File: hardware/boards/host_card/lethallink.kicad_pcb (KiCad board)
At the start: 6 copper layers, 121.2 x 98.4 mm, 220 parts, among them J1 PCIe-x4, J2 USB3_Micro_B_Amphenol, J3 Conn_02x05_Odd_Even, J4 Conn_02x04_Odd_Even, J5 Conn_02x04_Odd_Even, J6 SODIMM_260, J7 Conn_02x04_Odd_Even, Q1 Q_NMOS_GSD, Q2 Q_NMOS_GSD, Q3 Q_NMOS_GSD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

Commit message: Fixed the missing bus connections to the FPGA for the USB3 PHY, and updated the PCB
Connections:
- U1 pad A2: /USB3 Interface/DQ12 -> /USB3 Interface/WE_D
- U1 pad A3: Net-(U1-PadA3) -> /USB3 Interface/DQ6
- U1 pad A4: Net-(U1-PadA4) -> /USB3 Interface/DQ0
- U1 pad A5: Net-(U1-PadA5) -> /USB3 Interface/DQ1
- U1 pad B1: /USB3 Interface/DQ13 -> /USB3 Interface/OE
- U1 pad B2: /USB3 Interface/DQ14 -> /USB3 Interface/ALE
- U1 pad B3: Net-(U1-PadB3) -> /USB3 Interface/DQ7
- U1 pad B4: Net-(U1-PadB4) -> /USB3 Interface/DQ5
- U1 pad B5: Net-(U1-PadB5) -> /USB3 Interface/DQ2
- U1 pad C1: /USB3 Interface/DQ8 -> Net-(U1-PadC1)
- U1 pad C2: /USB3 Interface/DQ15 -> Net-(U1-PadC2)
- U1 pad C3: Net-(U1-PadC3) -> /USB3 Interface/DQ10
- U1 pad C4: Net-(U1-PadC4) -> /USB3 Interface/DQ4
- U1 pad C5: Net-(U1-PadC5) -> /USB3 Interface/DQ3
- U1 pad D1: /USB3 Interface/DQ9 -> Net-(U1-PadD1)
- U1 pad D2: /USB3 Interface/DQ10 -> Net-(U1-PadD2)
- U1 pad D3: Net-(U1-PadD3) -> /USB3 Interface/DQ11
- U1 pad D5: Net-(U1-PadD5) -> /USB3 Interface/DQ9
- U1 pad E1: /USB3 Interface/DQ11 -> Net-(U1-PadE1)
- U1 pad E2: /USB3 Interface/DQ3 -> Net-(U1-PadE2)
- U1 pad E3: /USB3 Interface/OE -> /USB3 Interface/DQ13
- U1 pad E4: Net-(U1-PadE4) -> /USB3 Interface/DQ8
- U1 pad E5: /USB3 Interface/ALE -> /USB3 Interface/DQ14
- U1 pad F1: Net-(U1-PadF1) -> /AUX Control/WAKE#
- U1 pad F2: /USB3 Interface/DQ2 -> Net-(U1-PadF2)
- U1 pad F3: /USB3 Interface/DQ1 -> Net-(U1-PadF3)
- U1 pad F4: /USB3 Interface/WE_D -> /USB3 Interface/DQ12
- U1 pad F5: Net-(U1-PadF5) -> /USB3 Interface/DQ15
- U1 pad G1: Net-(U1-PadG1) -> /AUX Control/PCIe_TRST#
- U1 pad G2: Net-(U1-PadG2) -> /AUX Control/CLKREQ#
- U1 pad G3: /USB3 Interface/DQ0 -> Net-(U1-PadG3)
- U1 pad G5: /USB3 Interface/DQ5 -> Net-(U1-PadG5)
- U1 pad H2: Net-(U1-PadH2) -> /AUX Control/PERST#
- U1 pad H3: /USB3 Interface/DQ7 -> Net-(U1-PadH3)
- U1 pad H4: /USB3 Interface/DQ4 -> Net-(U1-PadH4)
- U1 pad H5: /USB3 Interface/DQ6 -> Net-(U1-PadH5)
- U1 pad J3: Net-(U1-PadJ3) -> /AUX Control/PCIe_SMCLK
- U1 pad J4: /AUX Control/PCIe_TMS -> Net-(U1-PadJ4)
- U1 pad J5: Net-(U1-PadJ5) -> /AUX Control/PCIe_SMDAT
- U1 pad K16: Net-(U1-PadK16) -> /DDR3 Cache/A6
- U1 pad K17: Net-(U1-PadK17) -> /DDR3 Cache/BA0
- U1 pad K4: /AUX Control/PCIe_TDO -> /AUX Control/PCIe_TCK
- U1 pad L1: /AUX Control/PCIe_SMCLK -> Net-(U1-PadL1)
- U1 pad L4: Net-(U1-PadL4) -> /AUX Control/PCIe_TDI
- U1 pad M1: /AUX Control/PCIe_SMDAT -> Net-(U1-PadM1)
- U1 pad M4: /AUX Control/PCIe_TCK -> /AUX Control/PCIe_TDO
- U1 pad N2: Net-(U1-PadN2) -> /AUX Control/PCIe_TMS
- U1 pad N4: /AUX Control/PCIe_TDI -> Net-(U1-PadN4)
- U1 pad P1: /AUX Control/CLKREQ# -> Net-(U1-PadP1)
- U1 pad P2: /AUX Control/WAKE# -> Net-(U1-PadP2)
- U1 pad P3: /AUX Control/PERST# -> Net-(U1-PadP3)
- U1 pad P4: /AUX Control/PCIe_TRST# -> Net-(U1-PadP4)

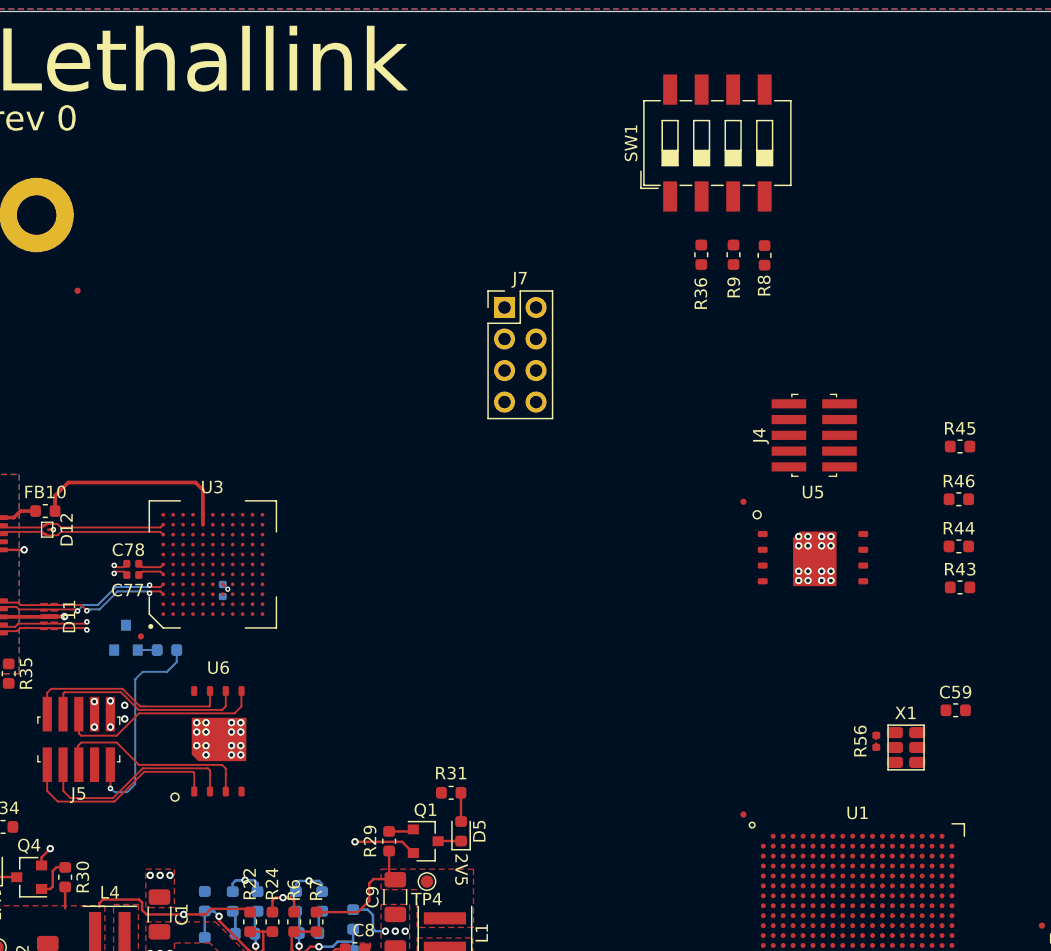
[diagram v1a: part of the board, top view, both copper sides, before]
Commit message: Swizzled the pins on the PHY bus to make routing to the FPGA nicer, also did the initial bus routing
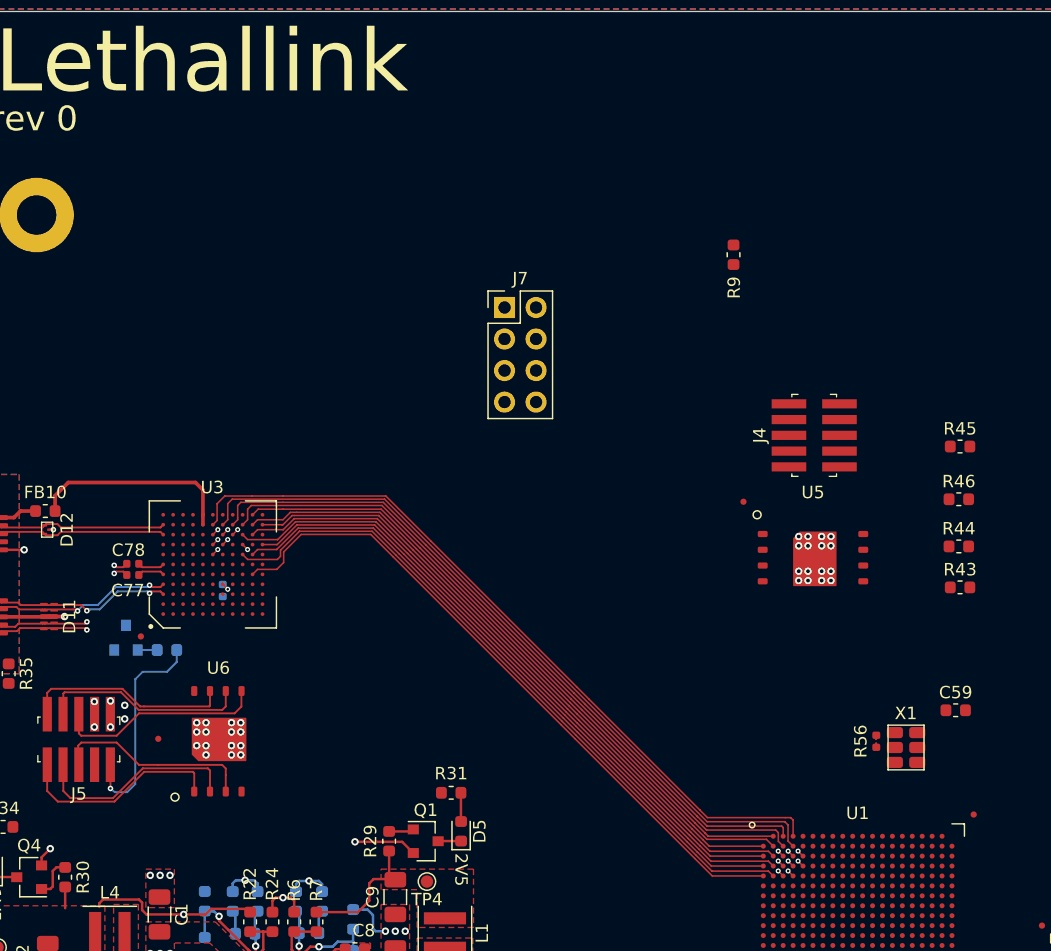
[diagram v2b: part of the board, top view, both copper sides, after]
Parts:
- removed R36, R8: 1k, Resistor_SMD:R_0603_1608Metric
- removed SW1: SW_DIP_x03, Button_Switch_SMD:SW_DIP_SPSTx04_Slide_6.7x11.72mm_W8.61mm_P2.54mm_LowProfile
- moved FID4 36.7 mm to (34.8, 74.3)
- moved FID3 18.5 mm to (100.5, 80.4)
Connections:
- U1 pad A2: /USB3 Interface/WE_D -> /USB3 Interface/DQ10
- U1 pad A5: /USB3 Interface/DQ1 -> Net-(U1-PadA5)
- U1 pad B1: /USB3 Interface/OE -> /USB3 Interface/DQ11
- U1 pad B2: /USB3 Interface/ALE -> /USB3 Interface/DQ12
- U1 pad B3: /USB3 Interface/DQ7 -> /USB3 Interface/DQ8
- U1 pad B4: /USB3 Interface/DQ5 -> /USB3 Interface/DQ3
- U1 pad B5: /USB3 Interface/DQ2 -> Net-(U1-PadB5)
- U1 pad C1: Net-(U1-PadC1) -> /USB3 Interface/DQ9
- U1 pad C2: Net-(U1-PadC2) -> /USB3 Interface/DQ13
- U1 pad C3: /USB3 Interface/DQ10 -> /USB3 Interface/DQ5
- U1 pad C4: /USB3 Interface/DQ4 -> /USB3 Interface/DQ7
- U1 pad C5: /USB3 Interface/DQ3 -> /USB3 Interface/DQ1
- U1 pad D1: Net-(U1-PadD1) -> /USB3 Interface/WE_D
- U1 pad D2: Net-(U1-PadD2) -> /Boot Config/~PHY_INT
- U1 pad D3: /USB3 Interface/DQ11 -> /USB3 Interface/DQ15
- U1 pad D5: /USB3 Interface/DQ9 -> /USB3 Interface/DQ4
- U1 pad E1: Net-(U1-PadE1) -> /USB3 Interface/ALE
- U1 pad E2: Net-(U1-PadE2) -> /USB3 Interface/OE
- U1 pad E3: /USB3 Interface/DQ13 -> /USB3 Interface/DQ14
- U1 pad E4: /USB3 Interface/DQ8 -> /USB3 Interface/DQ2
- U1 pad E5: /USB3 Interface/DQ14 -> Net-(U1-PadE5)
- U1 pad F4: /USB3 Interface/DQ12 -> Net-(U1-PadF4)
- U1 pad F5: /USB3 Interface/DQ15 -> Net-(U1-PadF5)
- U1 pad R4: Net-(R8-Pad2) -> GND
- U1 pad U4: Net-(R36-Pad2) -> GND
- U3 pad K8: /Boot Config/~PHY_INT -> Net-(U3-PadK8)
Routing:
- net /USB3 Interface/DQ0: track 0.00 -> 60.6 mm
- net /USB3 Interface/DQ1: track 0.00 -> 60.0 mm, vias 0 -> 2
- net /USB3 Interface/DQ3: track 0.00 -> 59.9 mm
- net /USB3 Interface/DQ4: track 0.00 -> 59.6 mm, vias 0 -> 2
- net /USB3 Interface/DQ2: track 0.00 -> 59.2 mm, vias 0 -> 2
- net /USB3 Interface/DQ5: track 0.00 -> 57.9 mm, vias 0 -> 2
- net /USB3 Interface/DQ6: track 0.00 -> 57.3 mm
- net /USB3 Interface/DQ15: track 0.00 -> 57.2 mm, vias 0 -> 2
- net /USB3 Interface/DQ7: track 0.00 -> 57.0 mm, vias 0 -> 2
- net /USB3 Interface/DQ8: track 0.00 -> 56.5 mm
- net /USB3 Interface/DQ14: track 0.00 -> 55.8 mm, vias 0 -> 2
- net /USB3 Interface/OE: track 0.00 -> 55.7 mm
- net /USB3 Interface/ALE: track 0.00 -> 54.4 mm
- net /USB3 Interface/DQ9: track 0.00 -> 53.9 mm
- net /USB3 Interface/DQ13: track 0.00 -> 53.7 mm
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
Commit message: Wiggling traces is hard
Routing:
- net /USB3 Interface/ALE: track 54.4 -> 39.6 mm
- net /USB3 Interface/DQ3: track 59.9 -> 47.6 mm
- net /USB3 Interface/DQ8: track 56.5 -> 45.9 mm
- net /USB3 Interface/OE: track 55.7 -> 46.8 mm
- net /USB3 Interface/DQ9: track 53.9 -> 45.4 mm
- net /Boot Config/~PHY_INT: track 53.2 -> 44.7 mm
- net /USB3 Interface/WE_D: track 53.3 -> 44.8 mm
- net /USB3 Interface/DQ6: track 57.3 -> 49.2 mm
- net /USB3 Interface/DQ12: track 53.5 -> 45.4 mm
- net /USB3 Interface/DQ11: track 51.7 -> 43.7 mm
- net /USB3 Interface/DQ13: track 53.7 -> 45.8 mm
- net /USB3 Interface/DQ10: track 53.1 -> 45.1 mm
- net /USB3 Interface/DQ0: track 60.6 -> 62.0 mm

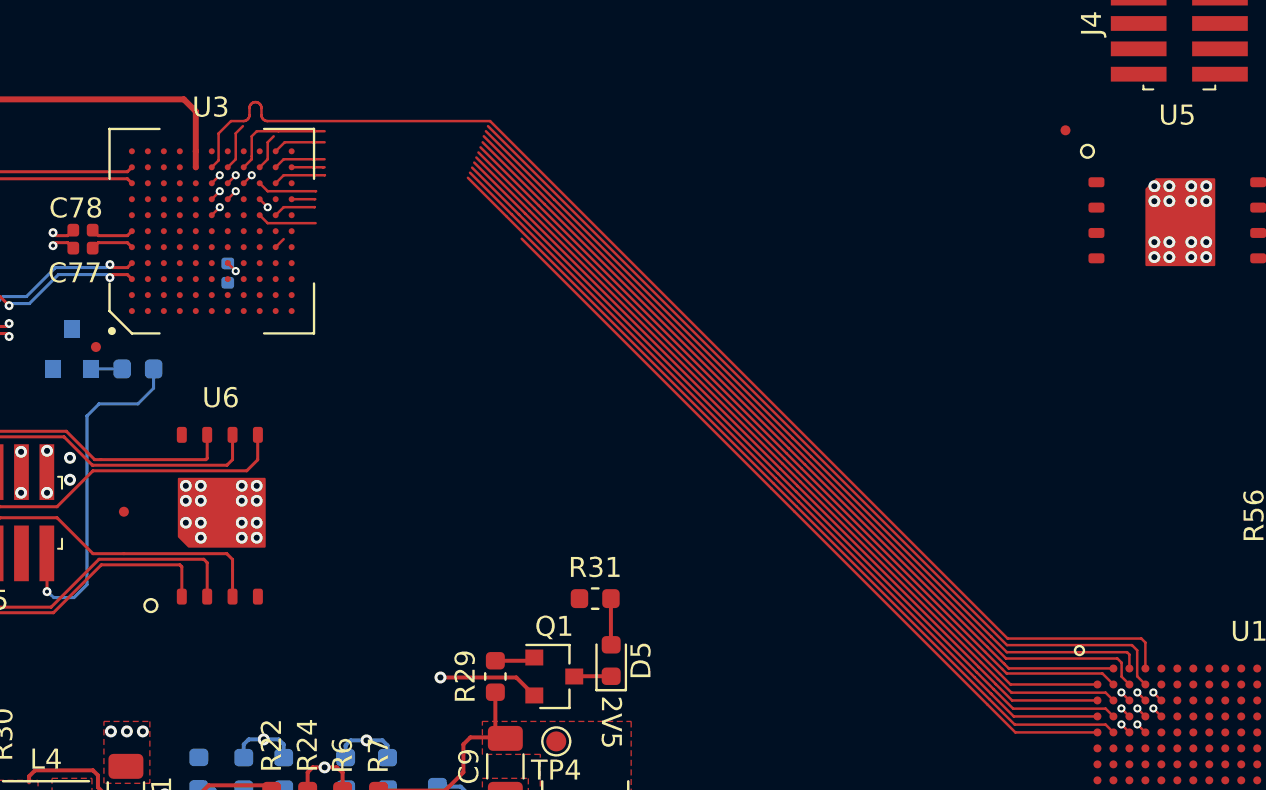
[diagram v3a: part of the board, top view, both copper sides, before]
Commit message: Created a suggested via layout for routing out the Cypress USB3 PHY
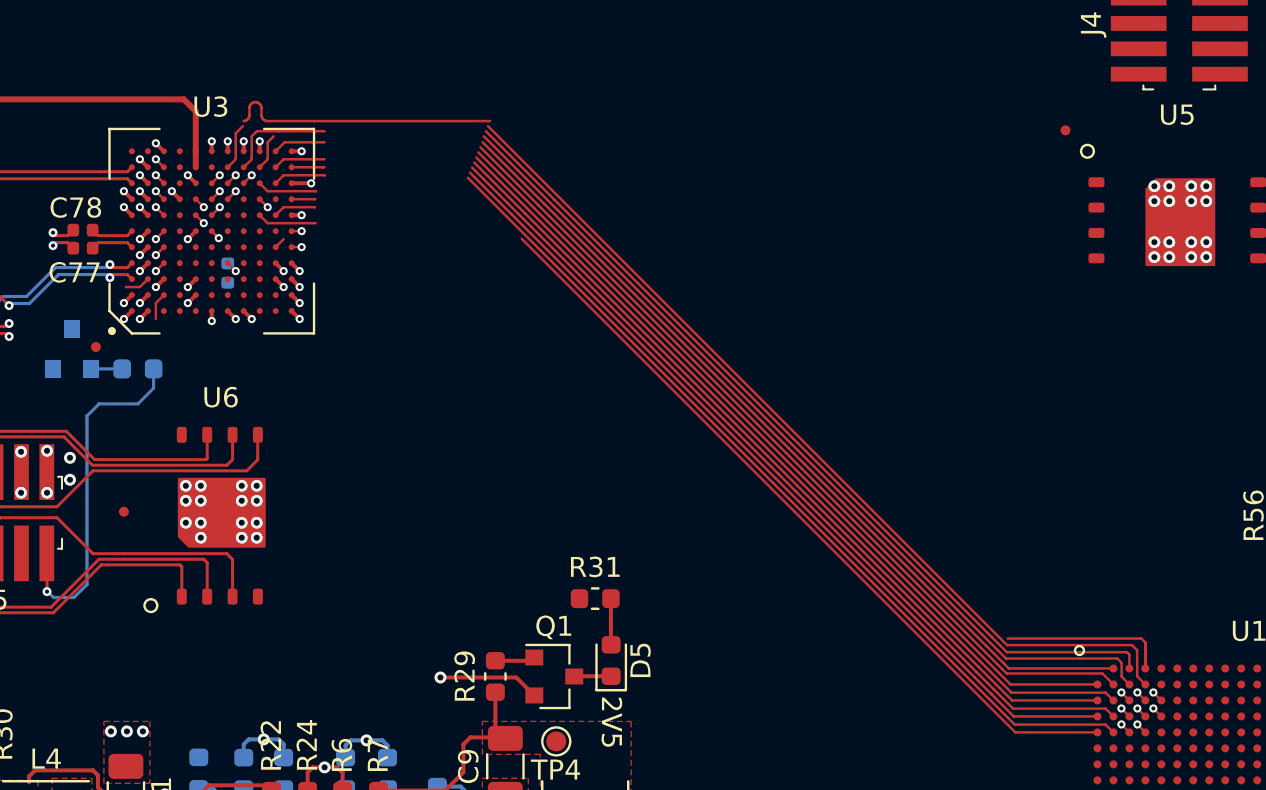
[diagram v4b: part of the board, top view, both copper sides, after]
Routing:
- net /USB3 Interface/DQ0: track 62.0 -> 23.3 mm
- net GND: track 64.6 -> 75.7 mm, vias 111 -> 131
- net +1V2: track 30.1 -> 36.1 mm, vias 2 -> 13
- net +1V8: track 33.5 -> 36.6 mm, vias 6 -> 11
- net /Boot Config/FPGA_DO: track 16.9 -> 18.3 mm
- net Net-(R53-Pad1): track 0.00 -> 1.27 mm
- net +3V3: track 4.17 -> 5.30 mm, vias 4 -> 6
- net Net-(Q7-Pad3): track 0.00 -> 0.57 mm, vias 0 -> 1
- net Net-(C55-Pad2): track 0.00 -> 0.57 mm, vias 0 -> 1
- net Net-(U3-PadC9): track 0.00 -> 0.57 mm, vias 0 -> 1
- net Net-(R52-Pad1): track 0.00 -> 0.57 mm, vias 0 -> 1
- net Net-(J3-Pad6): track 0.00 -> 0.57 mm, vias 0 -> 1
- net Net-(C56-Pad2): track 0.00 -> 0.57 mm, vias 0 -> 1
- net /Boot Config/~FPGA_CS: track 0.00 -> 0.57 mm, vias 0 -> 1
- net /Boot Config/TMS: track 0.00 -> 0.57 mm, vias 0 -> 1
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
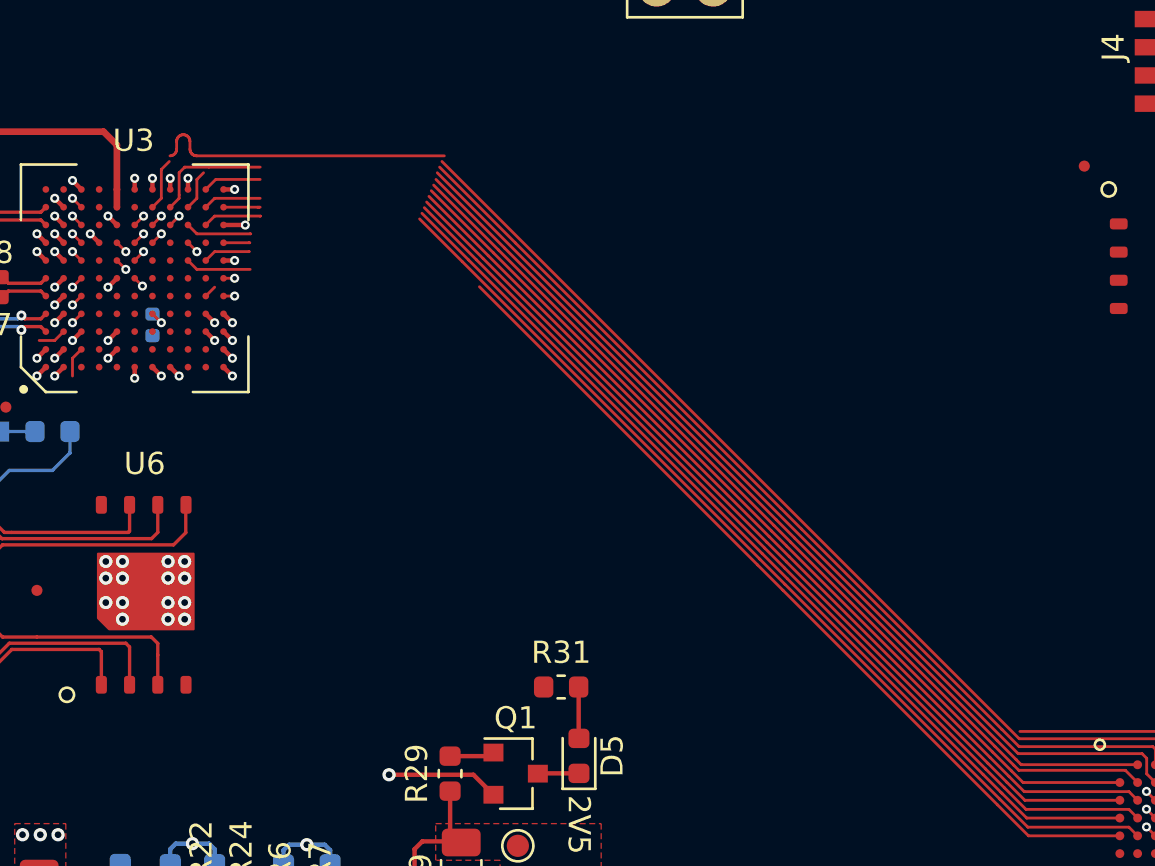
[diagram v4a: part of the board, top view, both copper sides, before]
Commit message: Fixed some traces that were munged w/ the PR
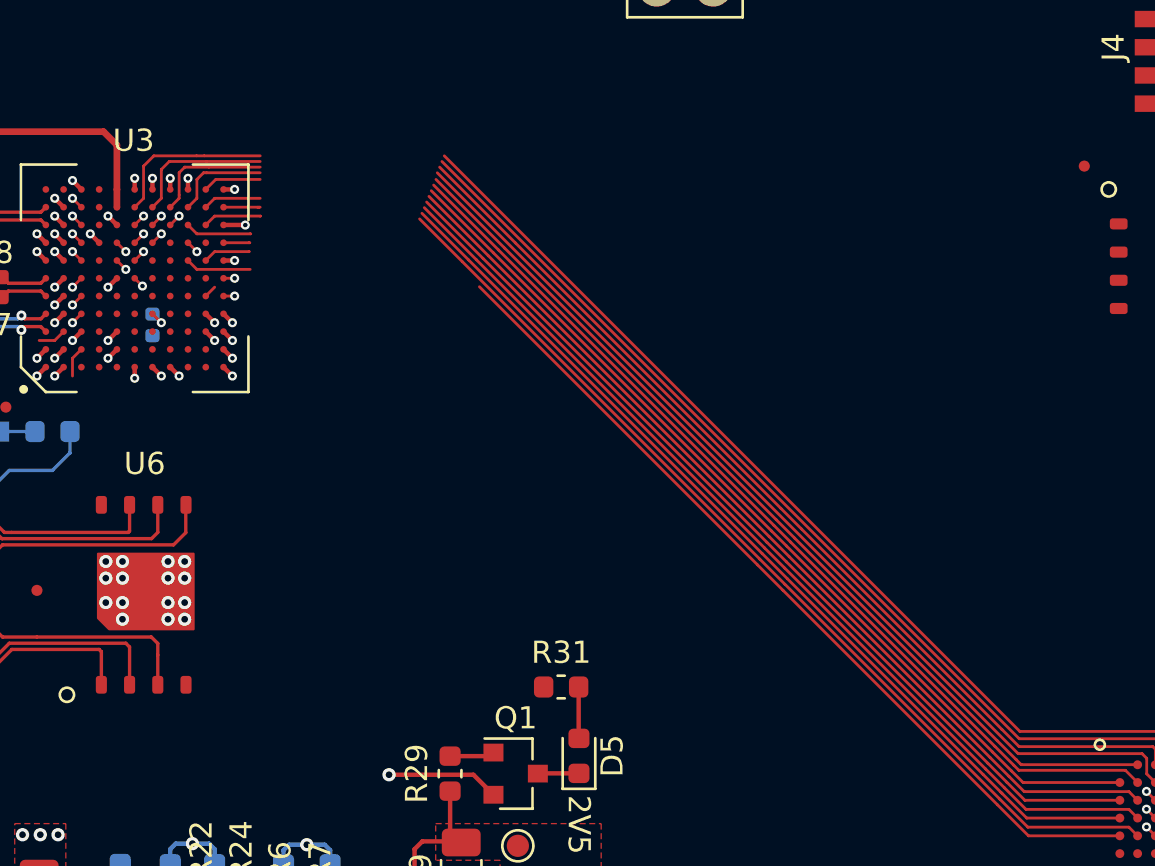
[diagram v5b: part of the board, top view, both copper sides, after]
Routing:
- net /USB3 Interface/DQ0: track 23.3 -> 53.7 mm
- net /USB3 Interface/DQ3: track 47.6 -> 51.7 mm
- net /USB3 Interface/DQ8: track 45.9 -> 48.5 mm
